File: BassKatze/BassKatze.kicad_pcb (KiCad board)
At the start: 2 copper layers, 55 x 54.9 mm, 43 parts, among them J1 Conn_01x02_Female, Q1 IRF7404, SW1 SW_Push, U1 ATmega328-AU, U2 MSGEQ7, U3 TP4056

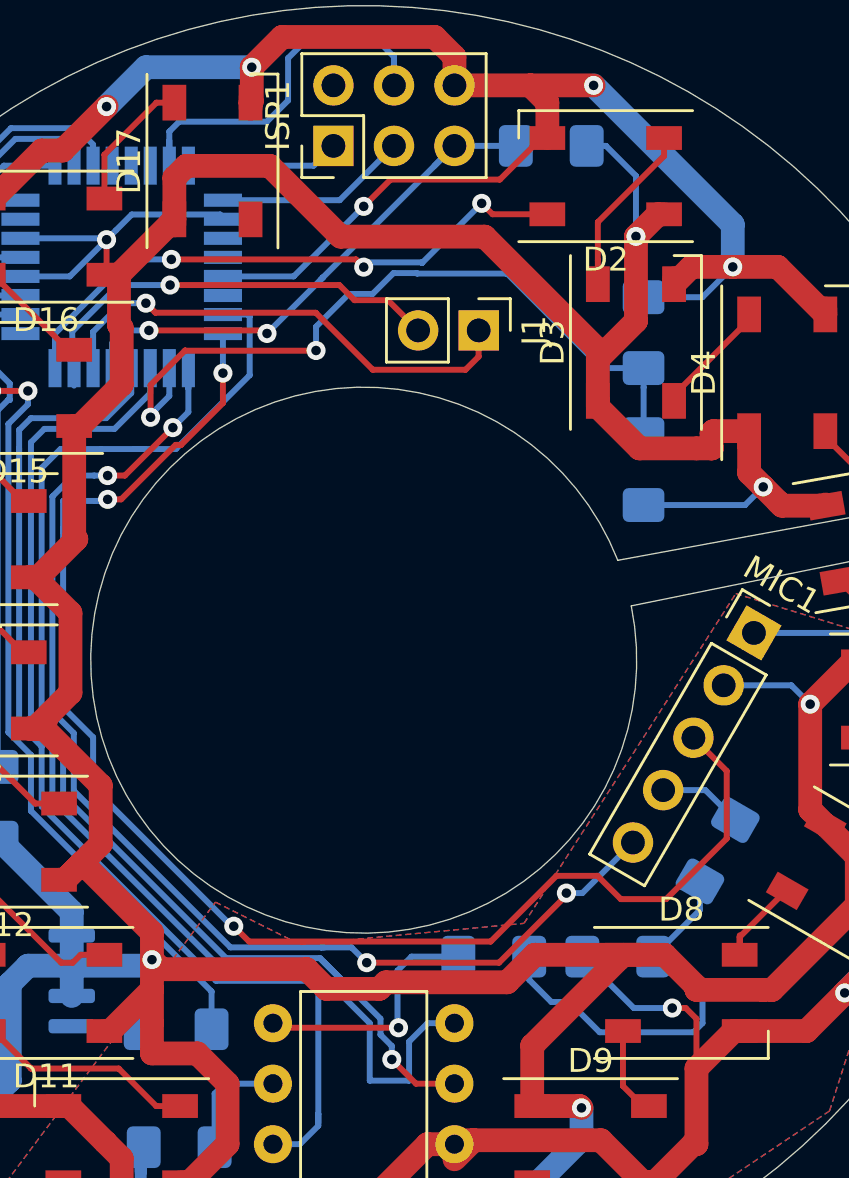
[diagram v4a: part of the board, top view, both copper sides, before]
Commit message: added missing voltage divider for analog signal to atmega
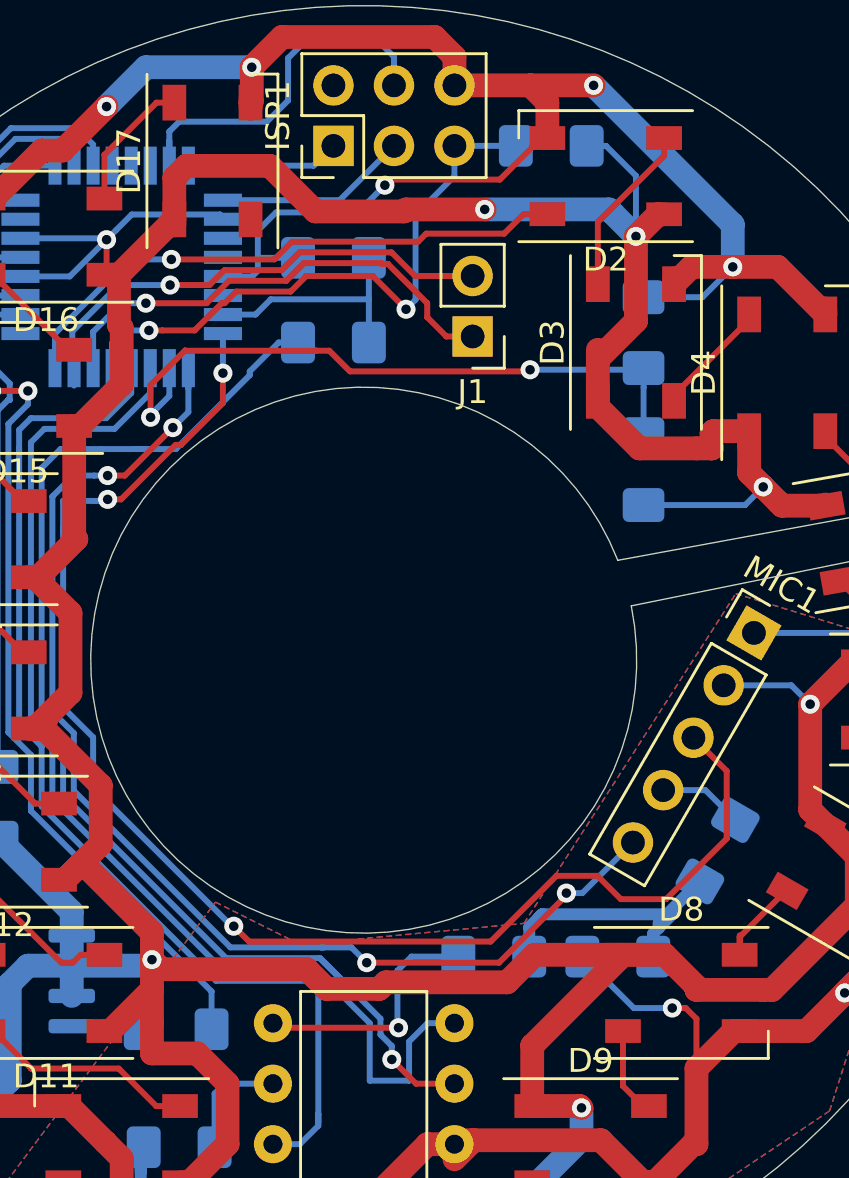
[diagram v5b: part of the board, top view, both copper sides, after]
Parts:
- added R10: 5KOhm, Resistor_SMD:R_1206_3216Metric_Pad1.42x1.75mm_HandSolder, B.Cu at (125.7, 113.7)
- added R9: 1KOhm, Resistor_SMD:R_1206_3216Metric_Pad1.42x1.75mm_HandSolder, B.Cu at (125.7, 110.1)
- R3: value 22KOhm -> 200KOhm
- moved J1 0.36 mm to (131.6, 113.4), turned to 180 degrees
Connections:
- U1 pad 23: RAW_Spectrum -> Net-(R10-Pad2)
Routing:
- net Net-(R10-Pad2): track 0.00 -> 10.7 mm
- net Net-(C3-Pad2): track 17.7 -> 13.0 mm
- net Net-(R7-Pad1): track 31.4 -> 28.2 mm
- net BAT-: track 263.4 -> 266.0 mm
- net Reset: track 22.9 -> 25.4 mm
- net Net-(J1-Pad2): track 18.4 -> 20.9 mm
- net RAW_Spectrum: track 54.5 -> 52.8 mm
- net LED1: track 25.9 -> 25.2 mm, vias 3 -> 1
- net PWR: track 226.2 -> 225.9 mm, vias 6 -> 7
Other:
- board text added: "BassKatze Rev 0.2"

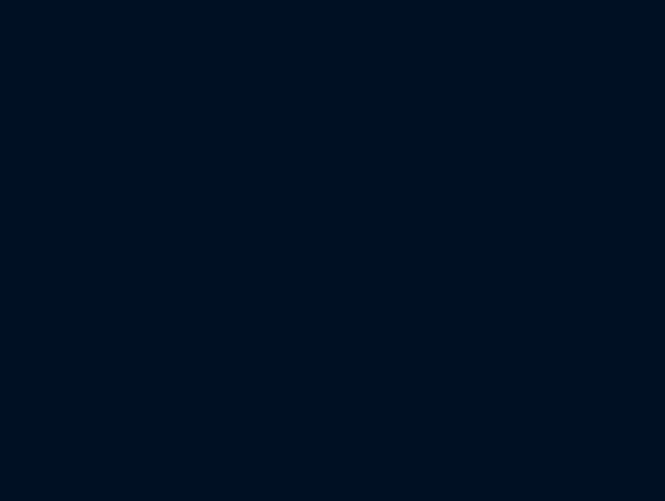
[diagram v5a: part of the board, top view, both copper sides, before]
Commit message: sync of annotations
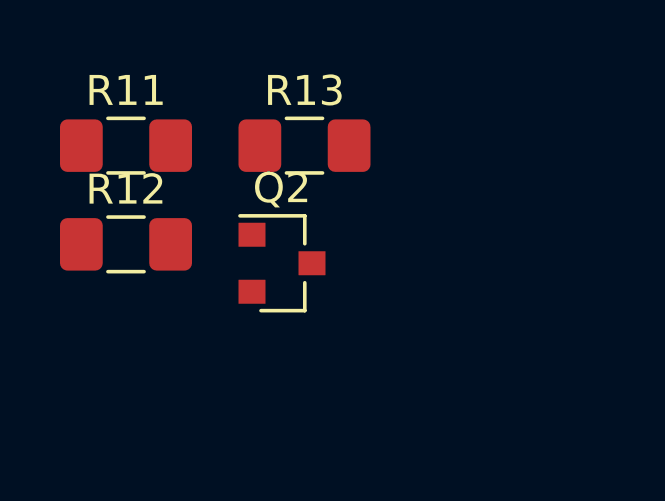
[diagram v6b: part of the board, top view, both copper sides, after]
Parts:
- added Q2: BSS138, Package_TO_SOT_SMD:SOT-23, F.Cu at (7.68, 5.07)
- added R11: 10KOhm, Resistor_SMD:R_1206_3216Metric_Pad1.42x1.75mm_HandSolder, F.Cu at (2.48, 1.15)
- added R12: 10KOhm, Resistor_SMD:R_1206_3216Metric_Pad1.42x1.75mm_HandSolder, F.Cu at (2.48, 4.44)
- added R13: 10KOhm, Resistor_SMD:R_1206_3216Metric_Pad1.42x1.75mm_HandSolder, F.Cu at (8.43, 1.15)
- R4: value 250Ohm -> 10KOhm
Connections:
- Q1 pad 1: PWR -> BAT+
- Q1 pad 2: PWR -> BAT+
- Q1 pad 3: PWR -> BAT+
- Q1 pad 5: BAT+ -> PWR
- Q1 pad 6: BAT+ -> PWR
- Q1 pad 7: BAT+ -> PWR
- Q1 pad 8: BAT+ -> PWR
- R4 pad 2: PWR_HOLD -> BAT+

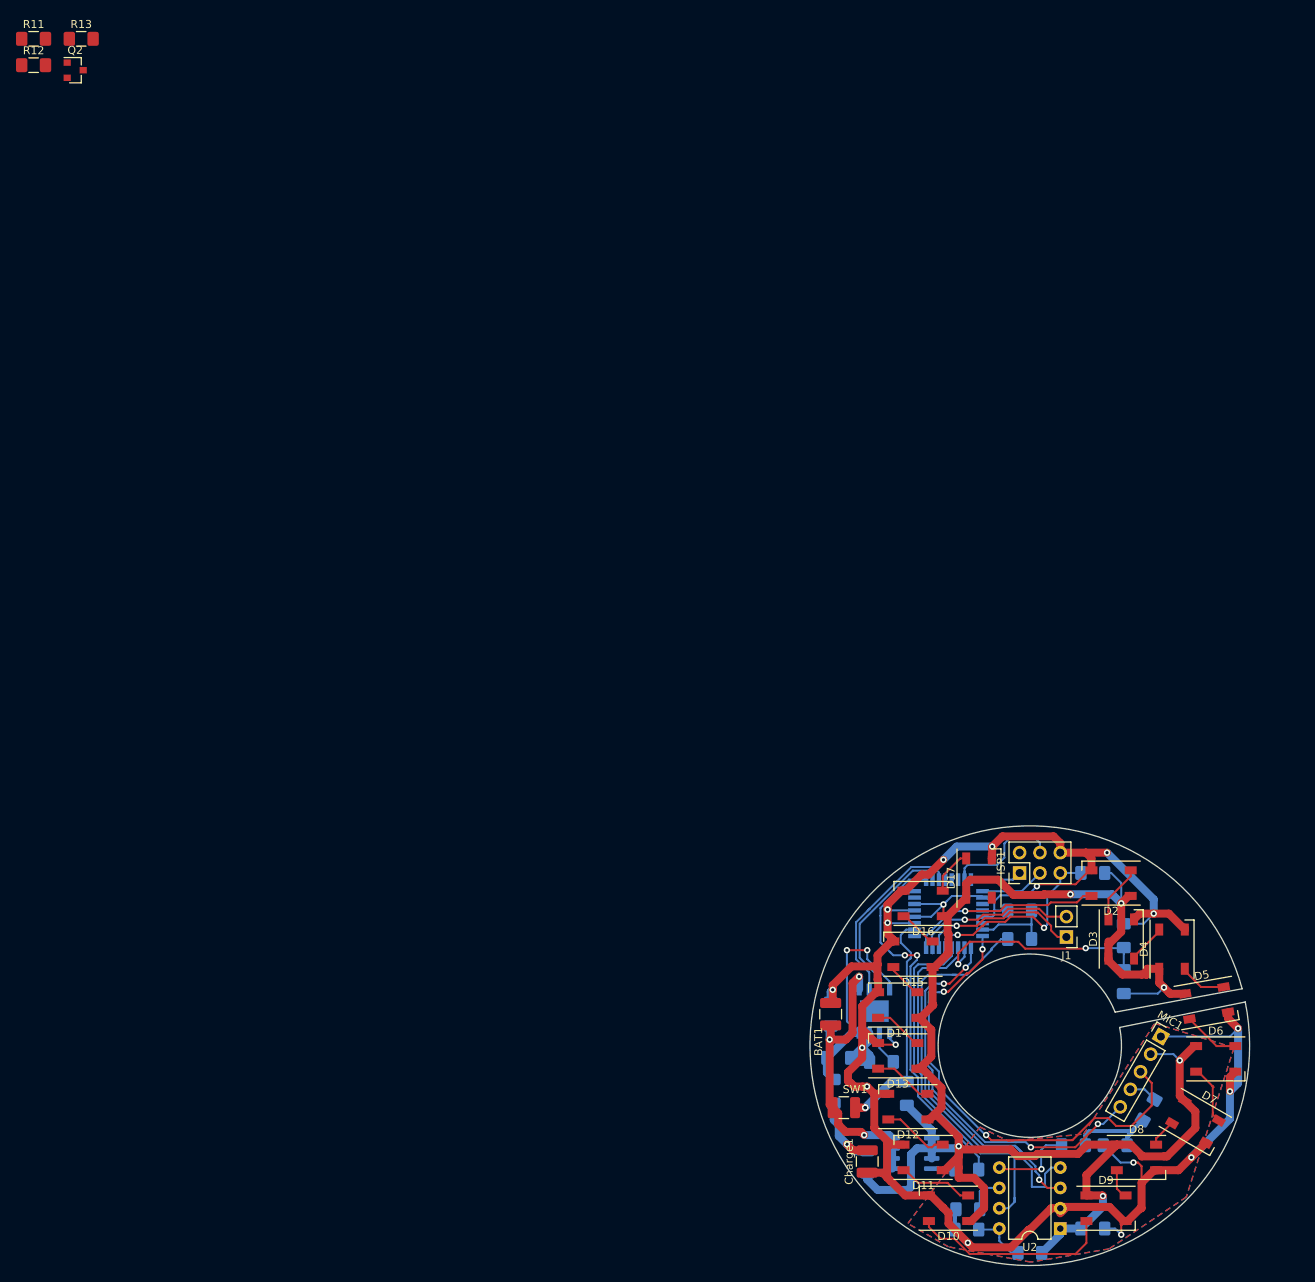
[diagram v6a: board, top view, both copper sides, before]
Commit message: fixed charging circuit cuttoff not working, updated pcb to schematic
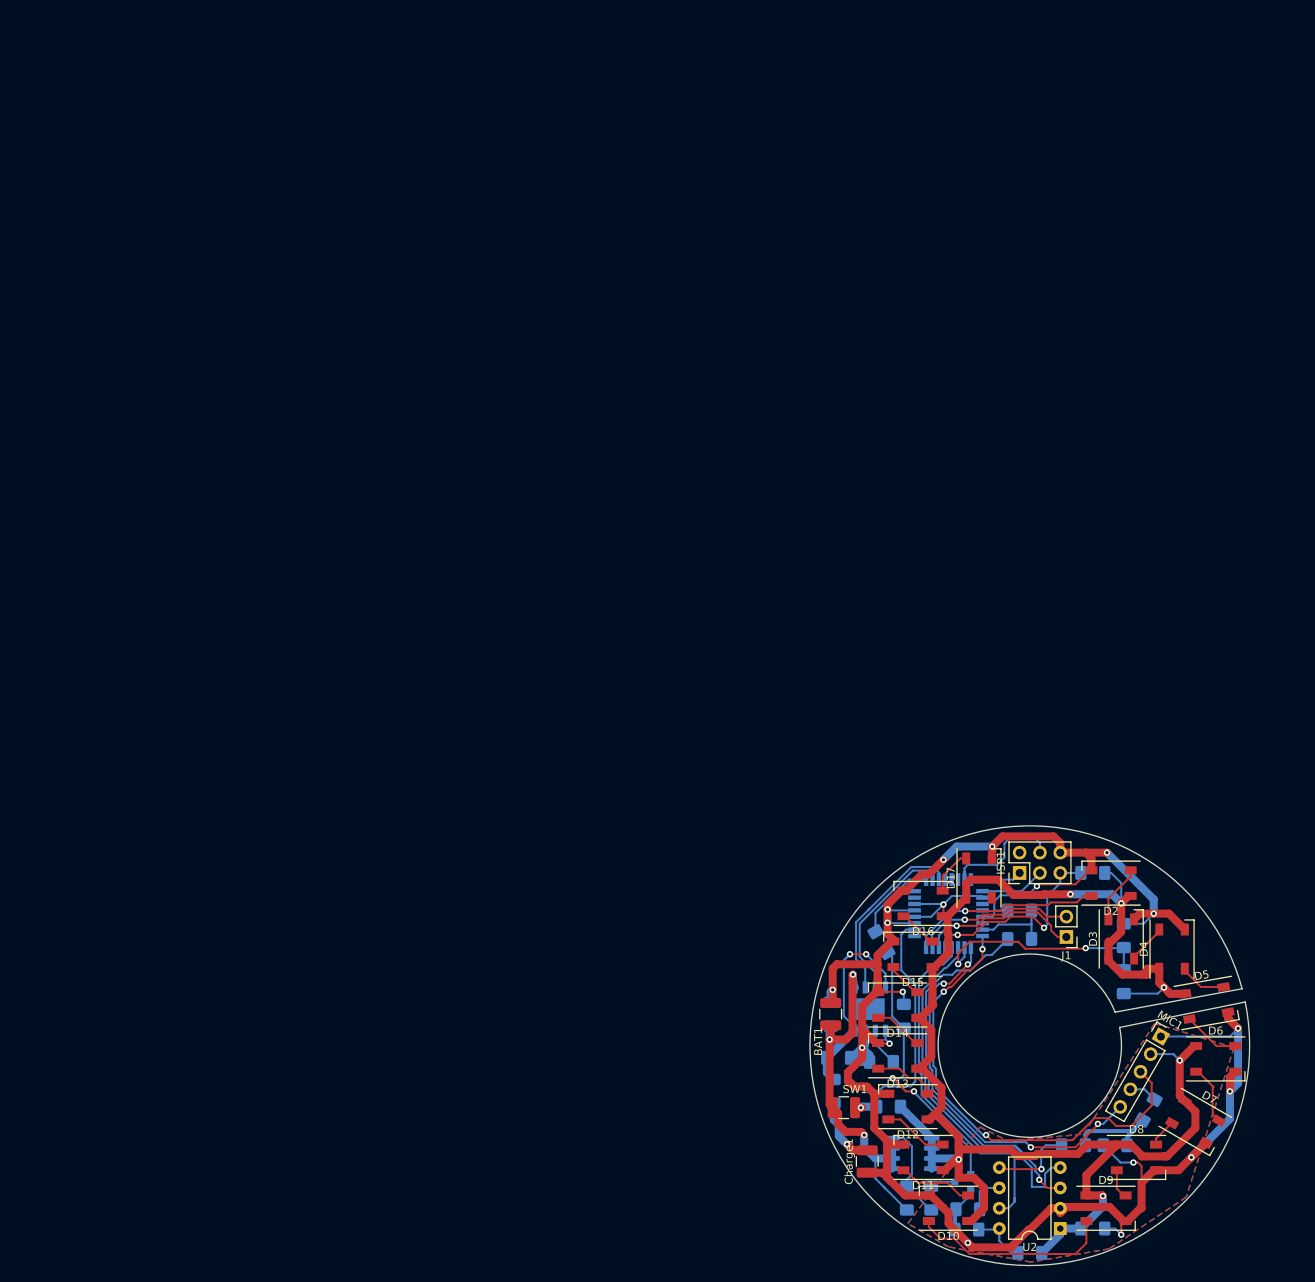
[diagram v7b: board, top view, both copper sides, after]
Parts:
- removed Charge_Powerup1: D, Diode_SMD:D_1206_3216Metric
- Q2, R12, R13: moved to B.Cu
- Re: renamed from R11; moved to B.Cu
- moved R13 179.7 mm to (114.7, 146.1), turned to 90 degrees
- moved Q2 177.8 mm to (118.6, 144.0), turned to 180 degrees
- moved R12 161.1 mm to (111.3, 123.3), turned to 90 degrees
- moved Re 154.9 mm to (108.5, 114.0), turned to 300 degrees
- moved R4 8.29 mm to (111.6, 146.1), turned to 270 degrees
- moved D1 2.82 mm to (109.3, 134.6), turned to 180 degrees
- moved U3 0.57 mm to (107.1, 122.4)
- turned Q1 to 0 degrees
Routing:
- net PWR_HOLD: track 47.4 -> 10.4 mm, vias 2 -> 0
- net Net-(Q2-Pad1): track 0.00 -> 34.4 mm, vias 0 -> 2
- net PWR: track 225.9 -> 213.4 mm
- net BAT+: track 38.1 -> 47.7 mm
- net Net-(Q1-Pad4): track 2.95 -> 12.4 mm
- net BAT-: track 266.0 -> 274.4 mm
- net Net-(Q2-Pad3): track 0.00 -> 3.16 mm
- net 5V_IN: track 11.6 -> 8.65 mm
- net EQ_Band: track 47.4 -> 45.3 mm
- net Net-(C1-Pad1): track 28.4 -> 26.3 mm
- net Button: track 30.4 -> 32.3 mm, vias 2 -> 1
- net EQ_Reset: track 45.8 -> 43.9 mm
- net Gain_Select: track 60.7 -> 59.3 mm
- net RAW_Spectrum: track 52.8 -> 51.8 mm
- net Attack_Select: track 51.3 -> 50.4 mm
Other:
- board text added: "BassKatze Rev 0.3"
- board text removed: "BassKatze Rev 0.2"

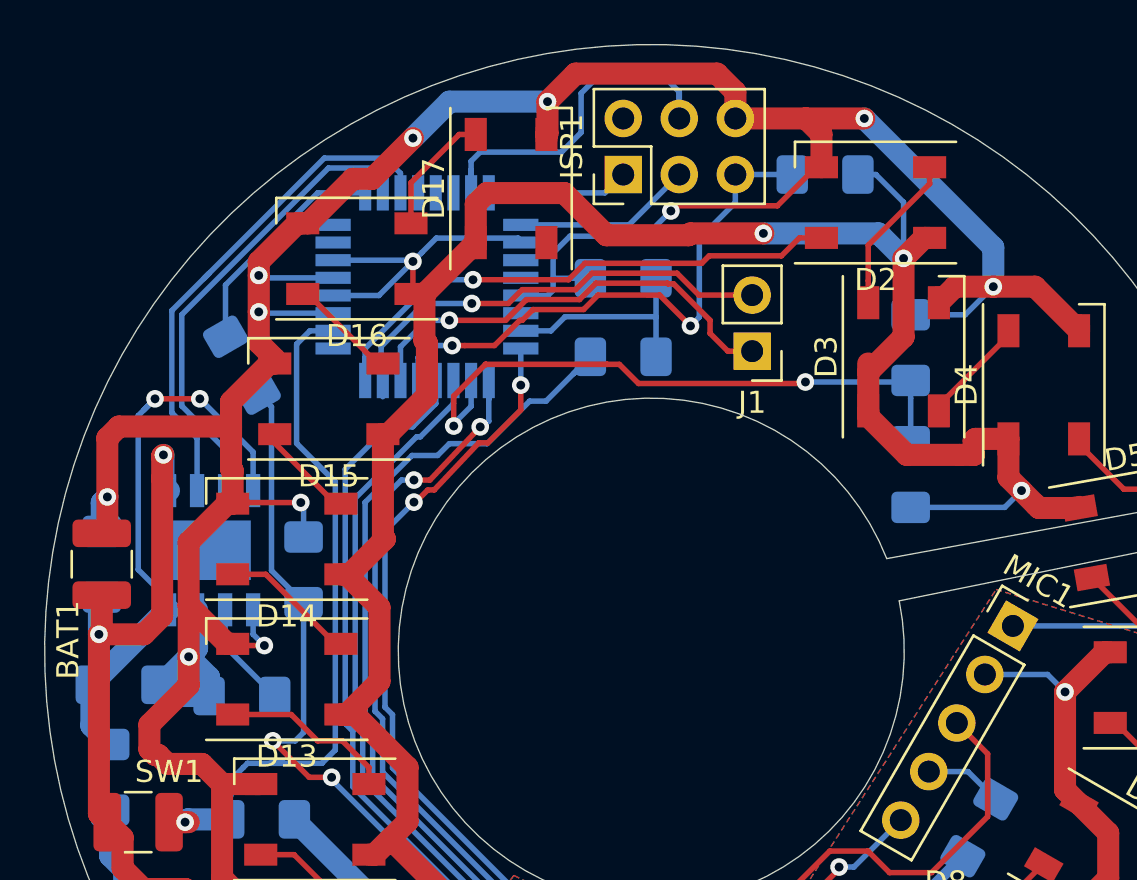
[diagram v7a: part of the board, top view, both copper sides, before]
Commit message: force poweron, if isp is connected
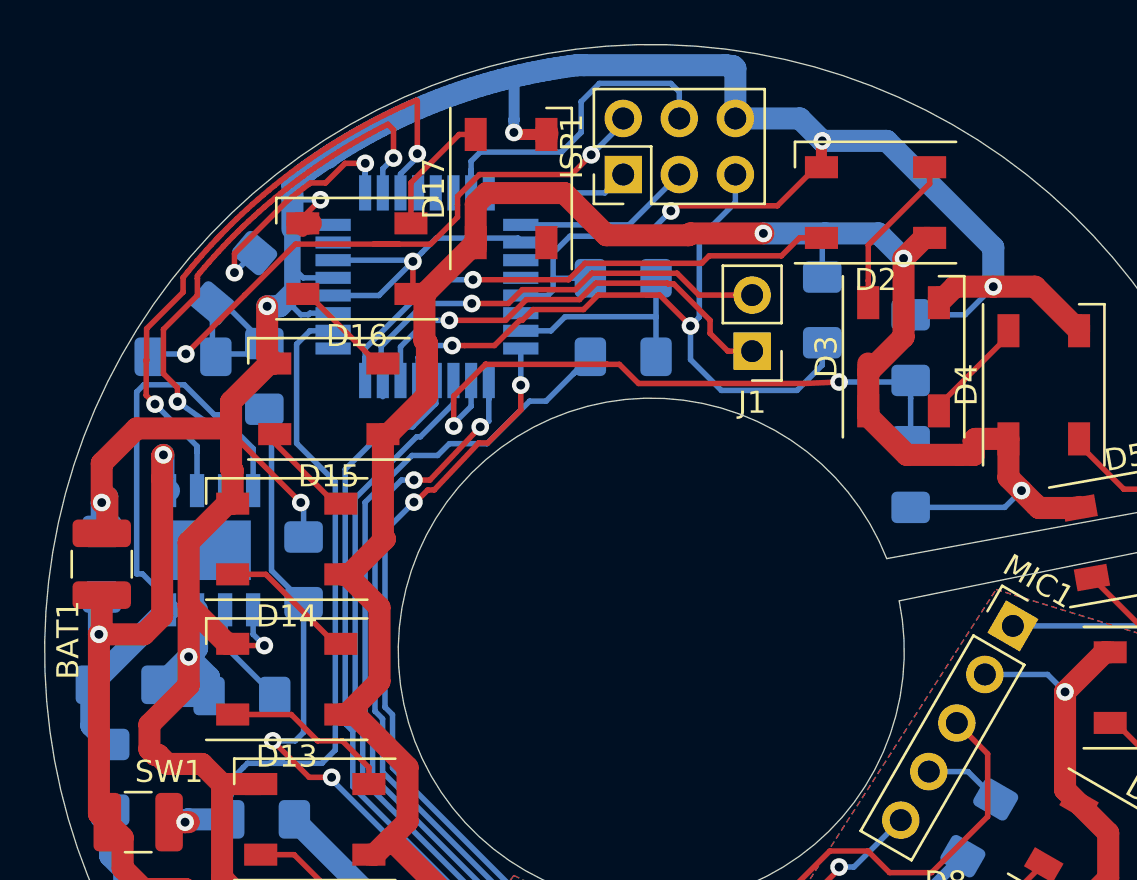
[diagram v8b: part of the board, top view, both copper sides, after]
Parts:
- removed Re: 10KOhm, Resistor_SMD:R_1206_3216Metric_Pad1.42x1.75mm_HandSolder
- added D18: D, Diode_SMD:D_1206_3216Metric_Pad1.42x1.75mm_HandSolder, B.Cu at (108.1, 110.1)
- added D19: D, Diode_SMD:D_1206_3216Metric_Pad1.42x1.75mm_HandSolder, B.Cu at (105.8, 113.7)
- added R11: 10KOhm, Resistor_SMD:R_1206_3216Metric_Pad1.42x1.75mm_HandSolder, B.Cu at (109.5, 114.6)
- moved R5 6.13 mm to (134.7, 111.5), turned to 90 degrees
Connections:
- ISP1 pad 2: (no net) -> 5V_Flash
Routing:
- net 5V_Flash: track 0.00 -> 27.5 mm, vias 0 -> 2
- net BAT-: track 274.4 -> 283.6 mm, vias 17 -> 16
- net Net-(D18-Pad1): track 0.00 -> 7.78 mm
- net Reset: track 25.4 -> 32.4 mm
- net STDBY: track 23.3 -> 29.8 mm, vias 0 -> 2
- net CHRG: track 21.7 -> 26.3 mm, vias 0 -> 2
- net PWR: track 213.4 -> 210.9 mm
- net Net-(C1-Pad1): track 26.3 -> 28.0 mm, vias 2 -> 0
- net MOSI: track 17.2 -> 15.6 mm
- net PWR_HOLD: track 10.4 -> 11.9 mm, vias 0 -> 2
- net Net-(Q2-Pad1): track 34.4 -> 33.5 mm
